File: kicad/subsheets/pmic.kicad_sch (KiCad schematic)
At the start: 22 parts, among them U2 TPS6521905RHBR

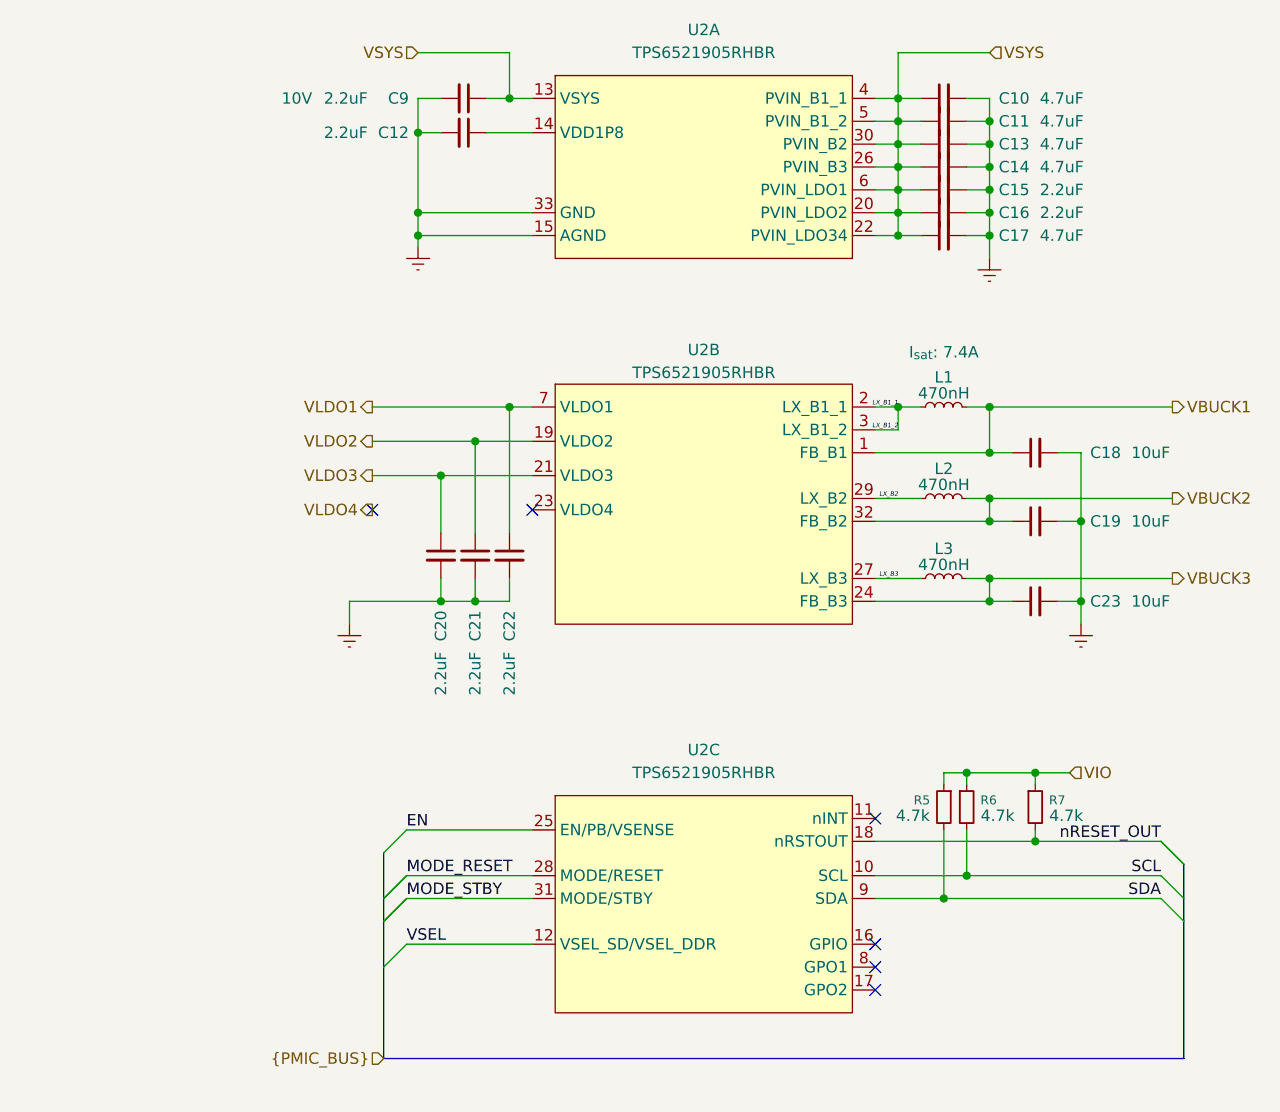
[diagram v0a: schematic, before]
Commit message: Footprint + silkscreen corrections
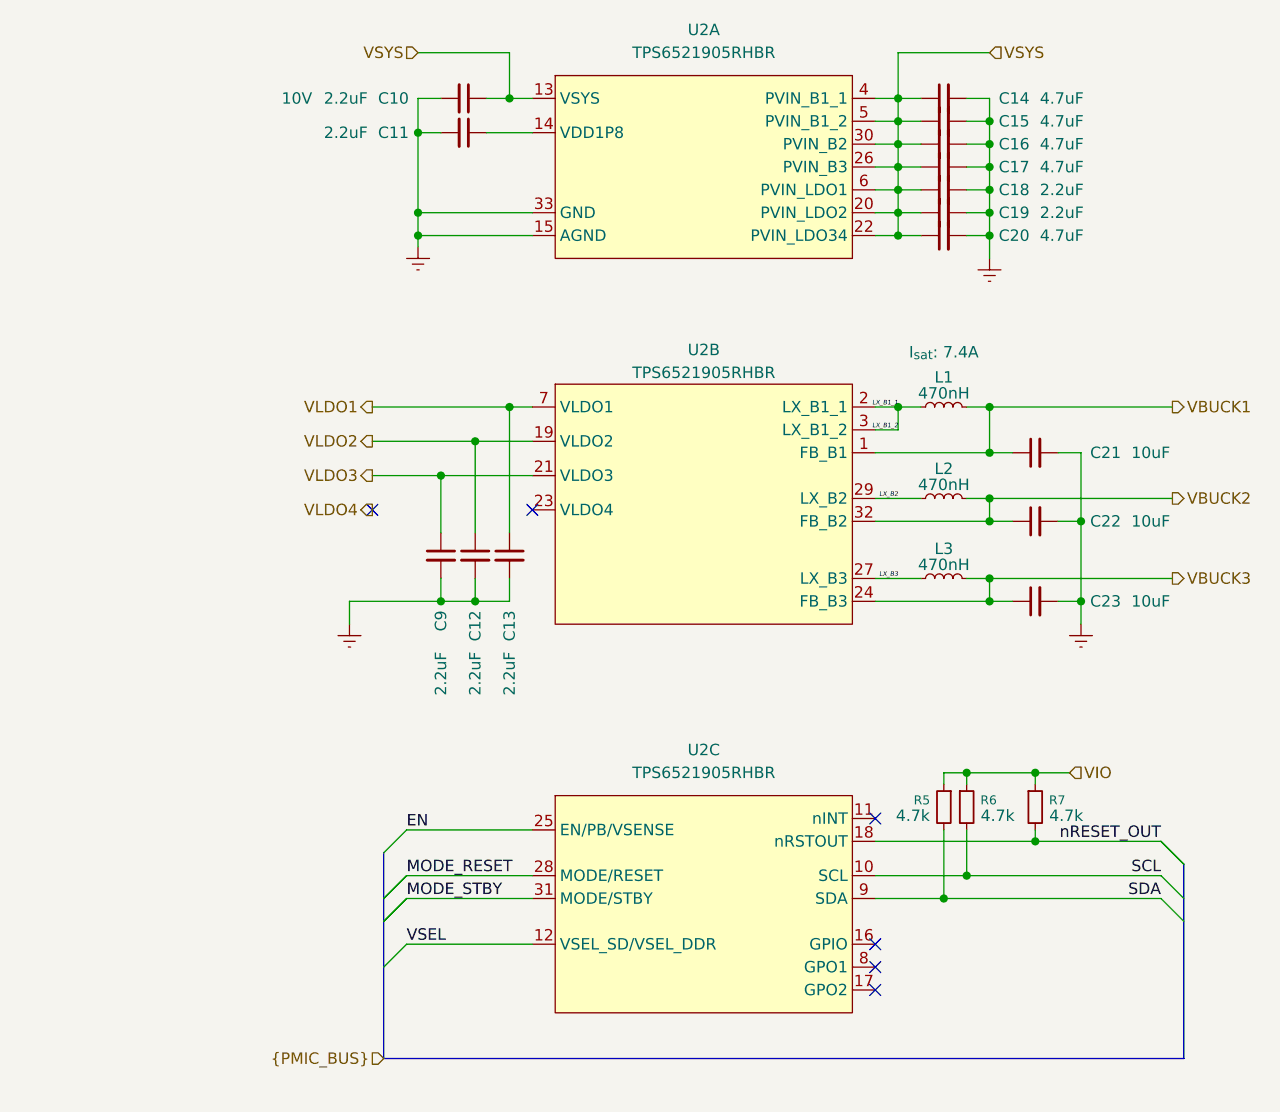
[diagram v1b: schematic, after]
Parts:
- C10: renamed from C9; now left out of the parts list
- C11: renamed from C12; now left out of the parts list
- C12: renamed from C21; now left out of the parts list
- C13: renamed from C22; now left out of the parts list
- C14: renamed from C10; now left out of the parts list
- C15: renamed from C11; now left out of the parts list
- C16: renamed from C13; now left out of the parts list
- C17: renamed from C14; now left out of the parts list
- C18: renamed from C15; now left out of the parts list
- C19: renamed from C16; now left out of the parts list
- C20: renamed from C17; now left out of the parts list
- C21: renamed from C18; now left out of the parts list
- C22: renamed from C19; now left out of the parts list
- C23, L1, L2, L3, R5, R6, R7, U2: now left out of the parts list
- C9: renamed from C20; now left out of the parts list

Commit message: Final changes before order
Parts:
- added R40, R41, R43: DNP, Resistor_SMD:R_0402_1005Metric, symbol Device:R_Small
- added R42: 10k, Resistor_SMD:R_0402_1005Metric, symbol Device:R_Small
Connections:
- net EN: now also R40.1, R41.2
- net GND: now also R41.1, R43.1
- net VIO: now also R40.2, R42.2
- net VSEL: now also R42.1, R43.2
- net LX_B1_1 renamed LX_B1

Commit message: Minor kicad changes
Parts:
- C10, C11, C12, C13, C18, C21, C22, C23, C9, L1, L2, L3, R43, R5, R6, R7, U2: BOARD_SIDE (none) -> Front; now in the parts list
- C14, C15, C16, C17, C19, C20, R40, R41: now in the parts list
- R42: BOARD_SIDE (none) -> Front
